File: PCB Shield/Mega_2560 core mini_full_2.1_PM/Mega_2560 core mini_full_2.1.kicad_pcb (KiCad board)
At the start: 2 copper layers, 89.5 x 59.7 mm, 136 parts, among them P1 2560-core, P10 RX1TX1, P11 Trim, P12 Stick_left, P13 Stick_right, P14 Switch, P15 LCD_I2C, P16 LCD, P17 BATT, P18 Ecolage, P19 Module_TX, P2 Clock, P20 TTL/RS232, P21 Sw_power, P22 JQ6500_28P, P23 Rot_1, P24 Rot_2, P25 Keys, P26 LCD_Alim, P27 HP, P28 5v/3,3v manches, P29 Sw_On, P3 Option, P30 MiniDCDC3A, P31 Pot2, P32 Pot1, P33 5V_CODERS, P4 Pot3, P5 Vibreur, P6 Micro_sd, P7 SPIX, P8 Audio, P9 SPI, Q1 IRLML5203, U1 74LVC1G3157GV, U2 TLP290, U3 TLP290, U4 PM5033, U5 LD1117S33TR, U6 MCP6004, U7 FM24W256, U8 DS3231SN

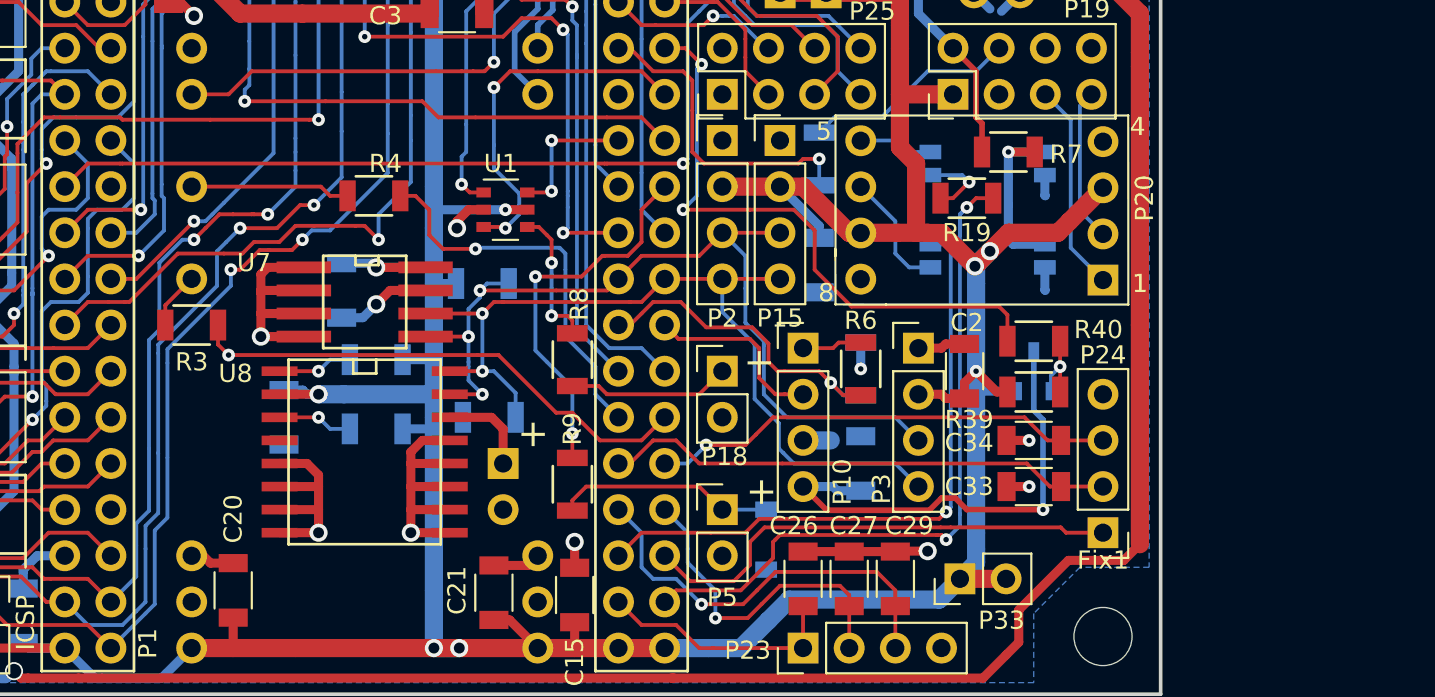
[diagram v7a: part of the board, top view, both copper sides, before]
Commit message: Update schematic é pcb files
-replace u2 and u3 by 2 74lvc1g3157gv
-remove p15 and p3
-add ftdi connector as p3
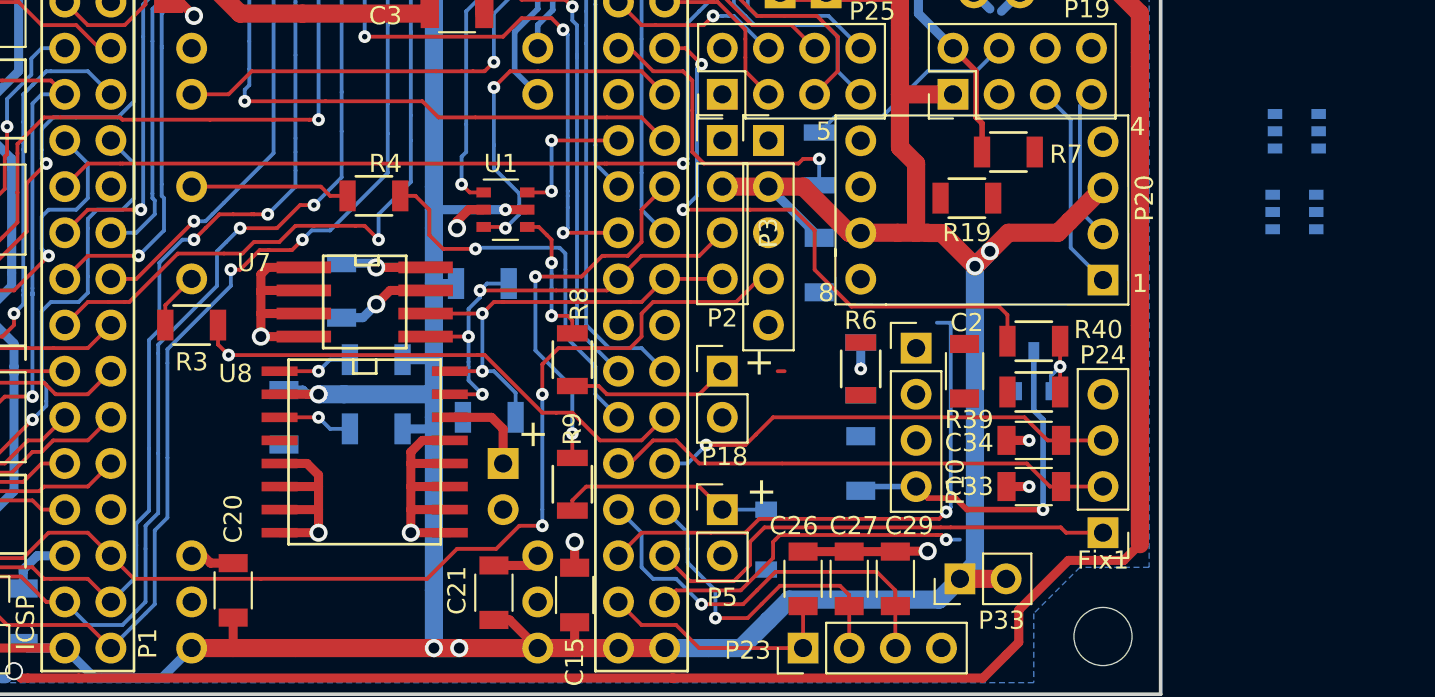
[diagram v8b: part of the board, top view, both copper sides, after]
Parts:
- removed P15: LCD_I2C, Pin_Headers:Pin_Header_Straight_1x04_Pitch2.54mm
- P2: value Clock -> LCD_I2C
- P3: value Option -> FTDI; footprint Pin_Headers:Pin_Header_Straight_1x04_Pitch2.54mm -> v2.1:Pin_Header_Straight_1x05_Pitch2.54mm
- U2: value TLP290 -> 74LVC1G3157GV; footprint MegaCore_Shield:SOP4 -> MegaCore_Shield:SOT-457
- U3: value TLP290 -> 74LVC1G3157GV; footprint anthoperso:SOP4 -> MegaCore_Shield:SOT-457
- moved U2 18.3 mm to (237.2, 90.6), turned to 0 degrees
- moved U3 17.1 mm to (237.1, 95.0), turned to 0 degrees
- moved P3 14.1 mm to (208.1, 91.1)
- moved P10 6.22 mm to (216.3, 102.5)
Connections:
- C2 pad 1: GND -> VCC
- C2 pad 2: VCC -> GND
- P1 pad RST: /OpenAVRc_CoreConnects/Isp_rst -> lsp_rst
- P3 pad 1: GND -> Net-(P3-Pad1)
- P3 pad 3: Sda -> lsp_rst
- P3 pad 4: Scl -> Net-(P3-Pad4)
- P9 pad 5: /OpenAVRc_CoreConnects/Isp_rst -> lsp_rst
- R7 pad 2: Net-(R7-Pad2) -> (no net)
- U2 pad 1: Net-(R7-Pad2) -> Net-(P20-Pad5)
- U2 pad 3: Net-(P20-Pad6) -> Net-(P3-Pad1)
- U3 pad 1: Net-(R7-Pad2) -> Net-(P20-Pad6)
- U3 pad 2: GND -> (no net)
- U3 pad 3: Net-(R19-Pad2) -> Net-(P3-Pad4)
- U3 pad 4: Net-(P20-Pad5) -> Net-(R19-Pad2)
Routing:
- net lsp_rst: track 0.00 -> 36.6 mm
- net Net-(P3-Pad4): track 0.00 -> 27.7 mm, vias 0 -> 2
- net Sda: track 49.4 -> 26.8 mm
- net Scl: track 48.1 -> 25.8 mm
- net Tele_RX: track 39.7 -> 18.4 mm, vias 2 -> 1
- net BT_Txd1: track 18.5 -> 0.00 mm, vias 1 -> 0
- net Net-(C24-Pad1): track 42.2 -> 26.9 mm
- net /OpenAVRc_CoreConnects/Isp_rst: track 14.2 -> 0.00 mm
- net Net-(R7-Pad2): track 10.4 -> 0.00 mm, vias 1 -> 0
- net BT_Rxd1: track 10.2 -> 0.00 mm
- net VCC: track 417.0 -> 408.2 mm, vias 15 -> 14
- net Net-(P20-Pad6): track 6.71 -> 0.00 mm
- net GND: track 137.9 -> 131.3 mm
- net Tele_TX: track 34.8 -> 30.3 mm
- net Net-(R19-Pad2): track 4.24 -> 0.00 mm, vias 1 -> 0
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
